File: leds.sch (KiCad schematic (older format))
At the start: 38 parts

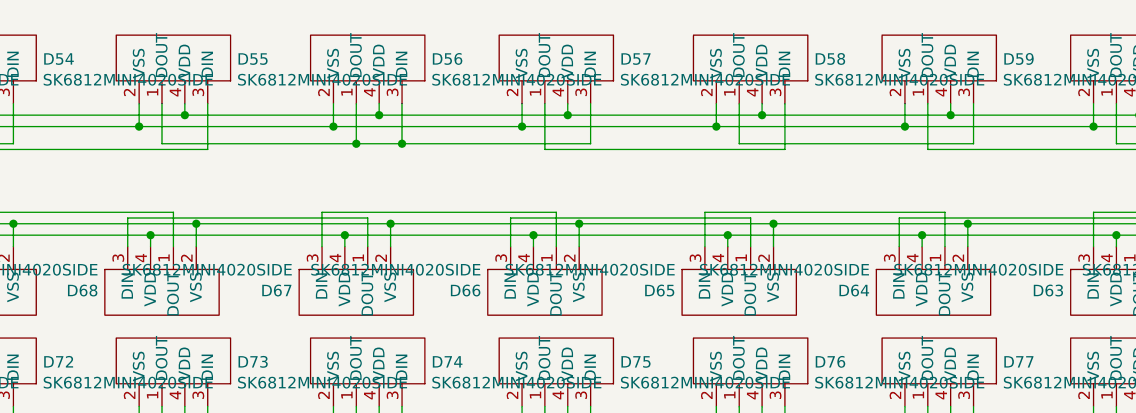
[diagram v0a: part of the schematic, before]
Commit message: corrected mising +5v trace and funky looking schematic on led 56
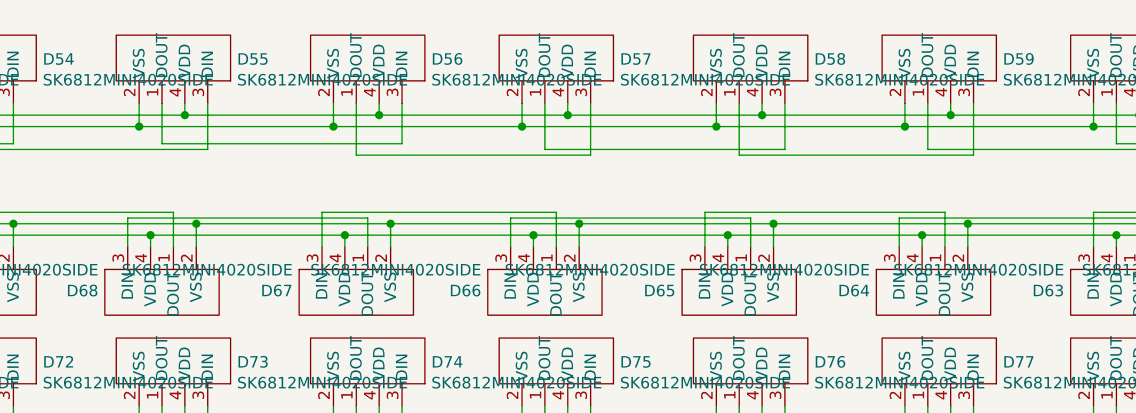
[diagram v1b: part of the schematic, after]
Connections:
- net at D55.1 (DOUT), D56.3 (DIN): no longer D56.1 (DOUT), D57.3 (DIN)
- new net: D56.1 (DOUT), D57.3 (DIN)
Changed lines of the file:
@@
 Connection ~ 5725 2150
-Wire Wire Line
-	6475 2100 6475 2275
-Wire Wire Line
-	7500 2275 7500 2100
-Wire Wire Line
-	5625 2275 6475 2275
-Connection ~ 6475 2275
-Wire Wire Line
-	6475 2275 6675 2275
-Connection ~ 6675 2275
-Wire Wire Line
-	6675 2275 7500 2275
 Wire Wire Line
 	6575 2150 7400 2150
@@
 	7300 2100 7300 2300
 Wire Wire Line
-	7300 2300 8350 2300
-Wire Wire Line
 	8350 2300 8350 2100
 Wire Wire Line
@@
 Connection ~ 7200 2200
 Wire Wire Line
-	8150 2100 8150 2275
-Wire Wire Line
-	8150 2275 9175 2275
-Wire Wire Line
-	9175 2275 9175 2100
-Wire Wire Line
 	8250 2150 9075 2150
 Wire Wire Line
@@
 	8975 2100 8975 2300
 Wire Wire Line
-	8975 2300 10000 2300
-Wire Wire Line
 	10000 2300 10000 2100
 Wire Wire Line
@@
 Wire Wire Line
 	4975 4875 4975 4675
+Wire Wire Line
+	5625 2275 6675 2275
+Wire Wire Line
+	6475 2100 6475 2325
+Wire Wire Line
+	6475 2325 7500 2325
+Wire Wire Line
+	7500 2100 7500 2325
+Wire Wire Line
+	7300 2300 8350 2300
+Wire Wire Line
+	8150 2325 9175 2325
+Wire Wire Line
+	8150 2100 8150 2325
+Wire Wire Line
+	9175 2100 9175 2325
+Wire Wire Line
+	8975 2300 10000 2300
 $EndSCHEMATC
